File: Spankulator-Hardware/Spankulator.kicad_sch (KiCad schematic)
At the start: 100 parts, among them J1 3.5mm Jack, J12 Arduino Socket, J13 Arduino Socket, J2 2x5 Header, J3 3.5mm Jack, J4 3.5mm Jack, J5 3.5mm Jack, J6 3.5mm Jack, J7 2x5 Header, J9 Display Header, Q1 2N3904, SW1 Adj, SW2 Push Button, SW3 Push Button, SW4 Push Button, SW5 Push Button, SW6 Push Button, SW7 Push Button, SW8 Push Button, U1 TL072CP, U2 CD4013BE, U3 TL072CP, U4 MC78L05_TO92, U5 LP2950-3.3_TO92, U6 MAX7480, U7 MB85RC256, U8 MCP6002-E/P

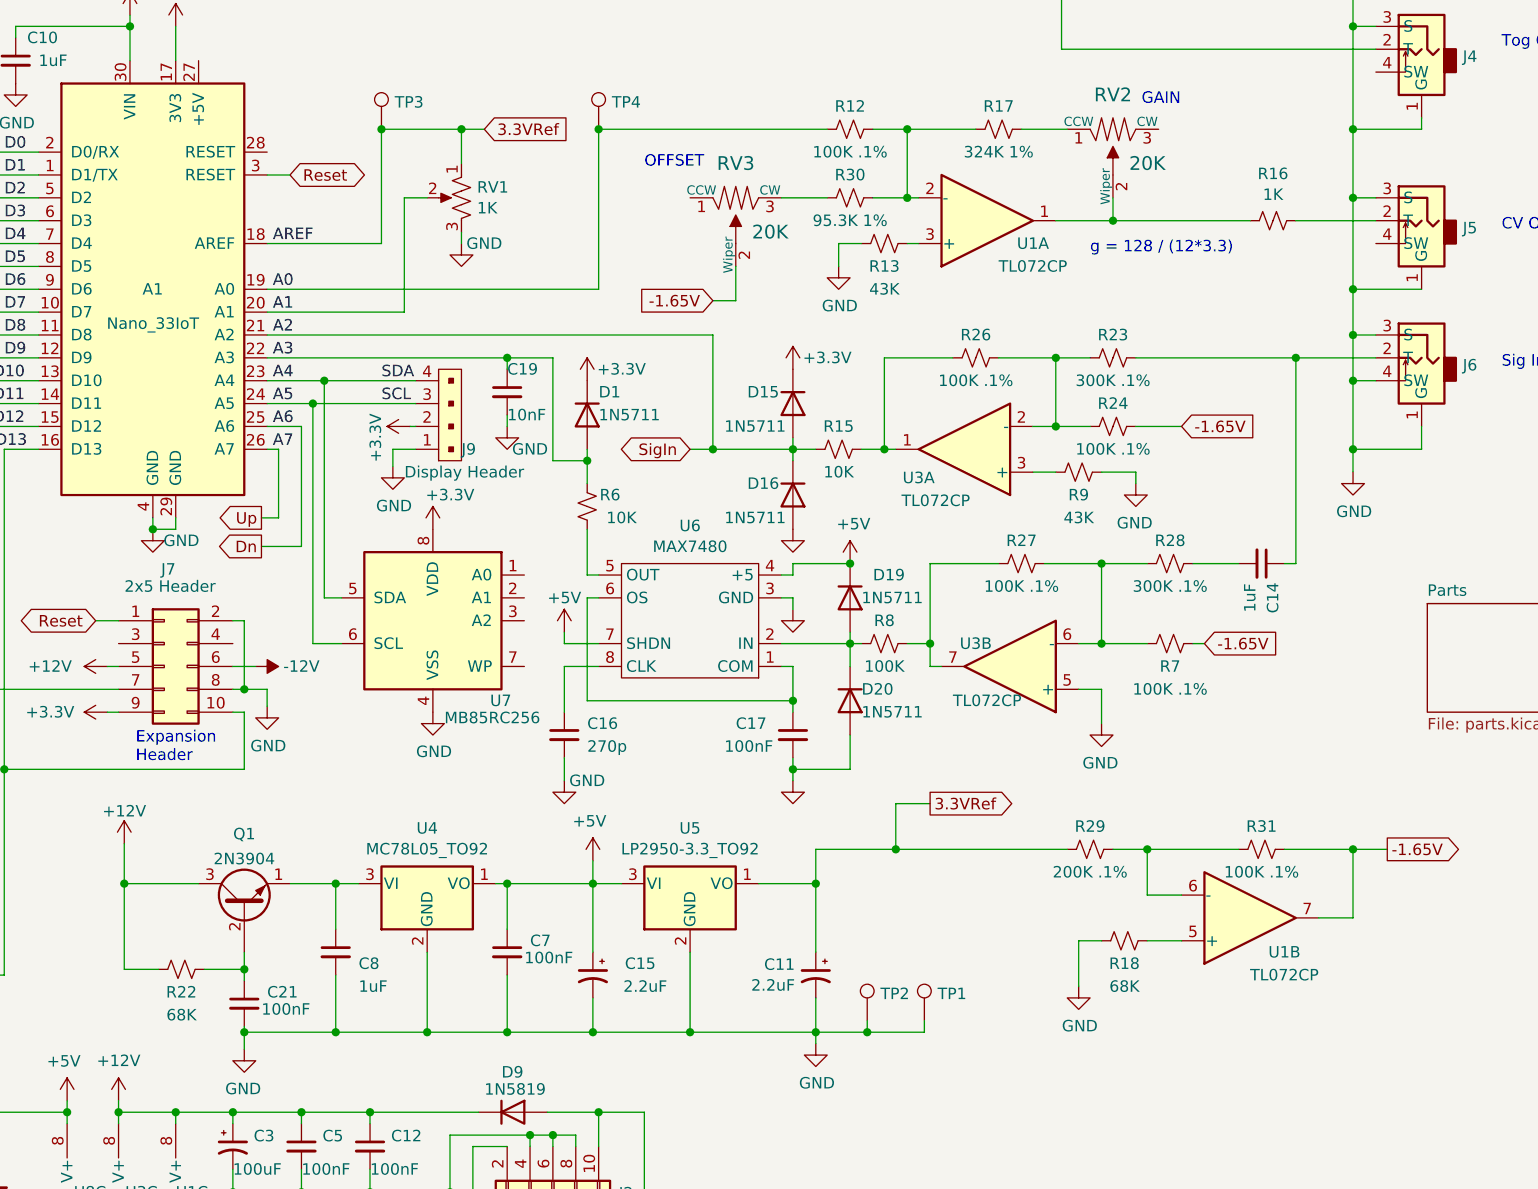
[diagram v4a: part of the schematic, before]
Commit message: Removes output resistor. Adjusts RC in reference filter
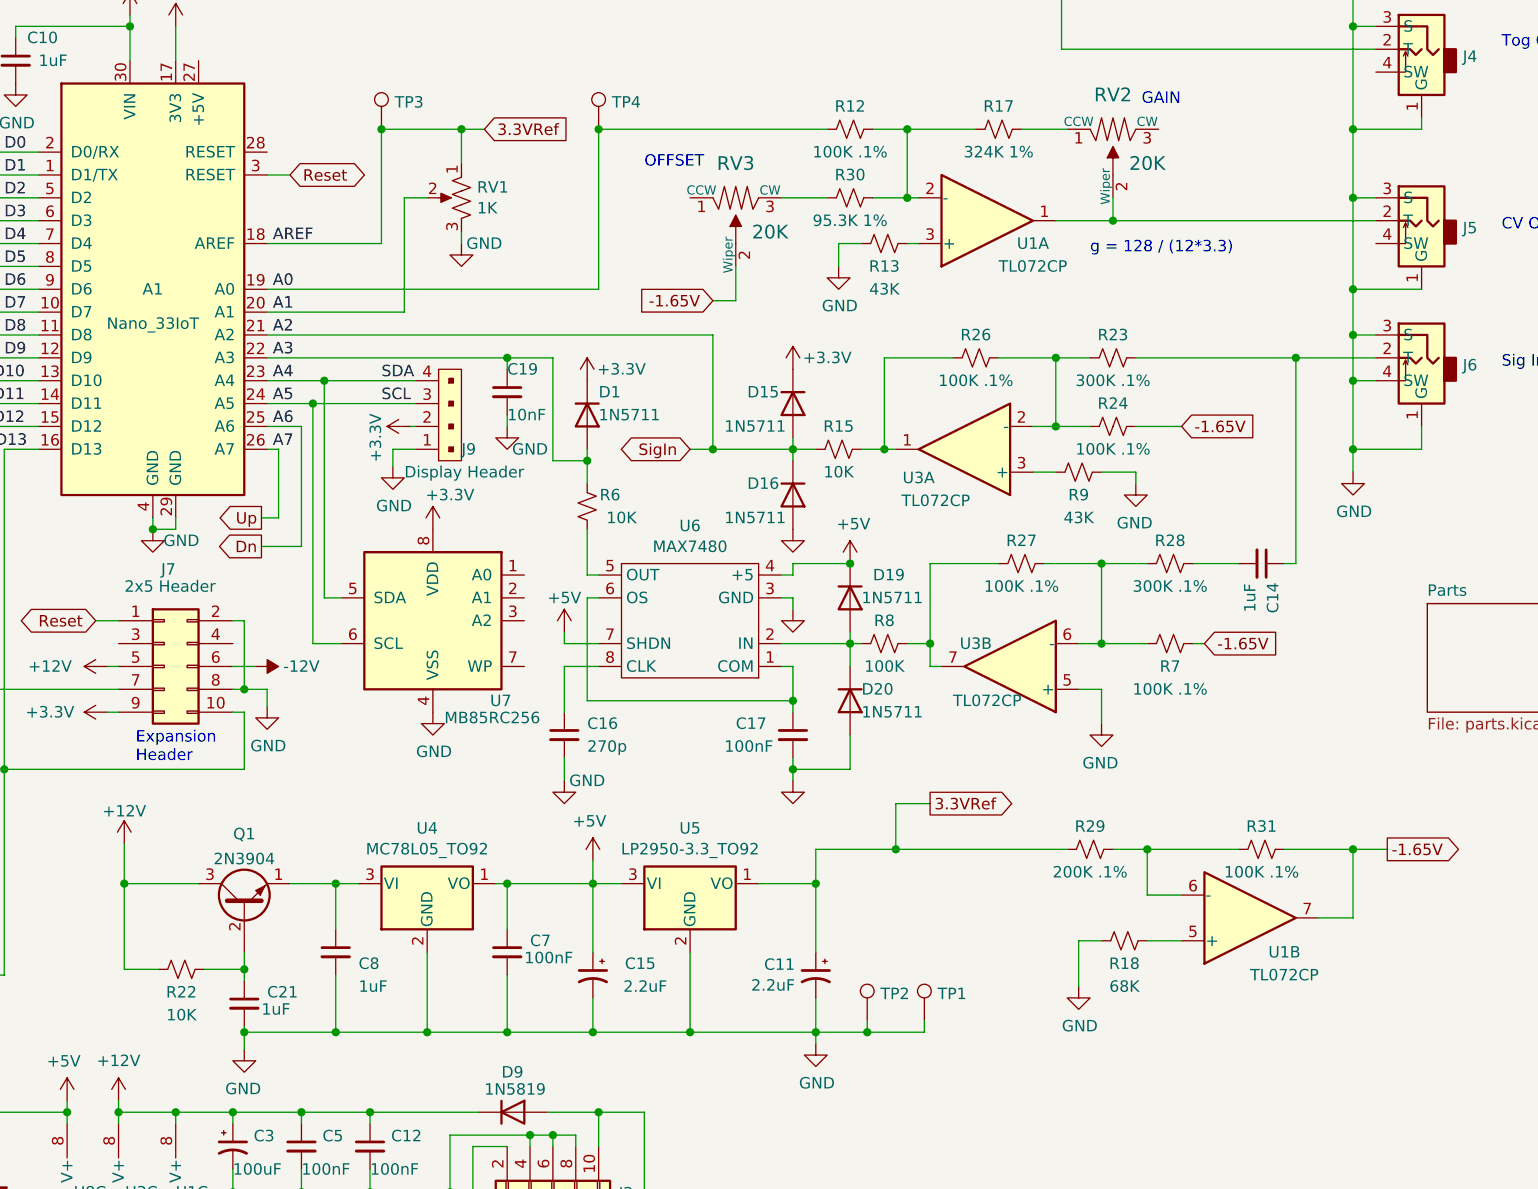
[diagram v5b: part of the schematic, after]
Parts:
- removed R16: 1K, Resistor_THT:R_Axial_DIN0207_L6.3mm_D2.5mm_P10.16mm_Horizontal, symbol Device:R_Small_US
- C21: value 100nF -> 1uF; Digi-Key Part 399-9877-1-ND -> 399-9886-1-ND; LCSC Part # C400087 -> C94708
- R22: value 68K -> 10K; Digi-Key Part CF14JT68K0CT-ND -> CF14JT10K0CT-ND; LCSC Part # C70783 -> C120103
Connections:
- net at RV2.2 (Wiper), U1.1: now also J5.2 (T)
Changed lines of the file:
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@@
     (stroke (width 0) (type default) (color 0 0 0 0))
   )
-  (wire (pts (xy 220.98 66.04) (xy 236.22 66.04))
-    (stroke (width 0) (type default) (color 0 0 0 0))
-  )
   (wire (pts (xy 219.71 93.98) (xy 223.52 93.98))
     (stroke (width 0) (type default) (color 0 0 0 0))
@@
     (stroke (width 0) (type default) (color 0 0 0 0))
   )
-  (wire (pts (xy 241.3 66.04) (xy 250.19 66.04))
+  (wire (pts (xy 220.98 66.04) (xy 250.19 66.04))
     (stroke (width 0) (type default) (color 0 0 0 0))
   )
@@
       (effects (font (size 1.27 1.27)) (justify left))
     )
-    (property "Value" "100nF" (id 1) (at 126.365 153.67 0)
+    (property "Value" "1uF" (id 1) (at 126.365 153.67 0)
       (effects (font (size 1.27 1.27)) (justify left))
     )
@@
       (effects (font (size 1.27 1.27)) hide)
     )
-    (property "Digi-Key Part" "399-9877-1-ND" (id 4) (at 124.46 153.035 0)
+    (property "Digi-Key Part" "399-9886-1-ND" (id 4) (at 124.46 153.035 0)
       (effects (font (size 1.27 1.27)) hide)
     )
-    (property "LCSC Part #" "C400087" (id 5) (at 124.46 153.035 0)
+    (property "LCSC Part #" "C94708" (id 5) (at 124.46 153.035 0)
       (effects (font (size 1.27 1.27)) hide)
     )
@@
     (in_bom yes) (on_board yes)
     (property "Reference" "R22" (id 0) (at 117.475 151.765 90))
-    (property "Value" "68K" (id 1) (at 117.475 154.305 90))
+    (property "Value" "10K" (id 1) (at 117.475 154.305 90))
     (property "Footprint" "Resistor_THT:R_Axial_DIN0207_L6.3mm_D2.5mm_P10.16mm_Horizontal" (id 2) (at 117.475 149.225 0)
       (effects (font (size 1.27 1.27)) hide)
@@
       (effects (font (size 1.27 1.27)) hide)
     )
-    (property "Digi-Key Part" "CF14JT68K0CT-ND" (id 4) (at 117.475 149.225 90)
+    (property "Digi-Key Part" "CF14JT10K0CT-ND" (id 4) (at 117.475 149.225 90)
       (effects (font (size 1.27 1.27)) hide)
     )
-    (property "LCSC Part #" "C70783" (id 5) (at 117.475 149.225 0)
-      (effects (font (size 1.27 1.27)) hide)
-    )
-    (pin "1")
-    (pin "2")
-  )
-  (symbol (lib_id "Device:R_Small_US") (at 238.76 66.04 270) (unit 1)
-    (in_bom yes) (on_board yes)
-    (property "Reference" "R16" (id 0) (at 238.76 60.833 90))
-    (property "Value" "1K" (id 1) (at 238.76 63.1444 90))
-    (property "Footprint" "Resistor_THT:R_Axial_DIN0207_L6.3mm_D2.5mm_P10.16mm_Horizontal" (id 2) (at 238.76 66.04 0)
-      (effects (font (size 1.27 1.27)) hide)
-    )
-    (property "Datasheet" "~" (id 3) (at 238.76 66.04 0)
-      (effects (font (size 1.27 1.27)) hide)
-    )
-    (property "Digi-Key Part" "CF14JT1K00CT-ND" (id 4) (at 238.76 66.04 90)
-      (effects (font (size 1.27 1.27)) hide)
-    )
-    (property "LCSC Part #" "C66649" (id 5) (at 238.76 66.04 0)
+    (property "LCSC Part #" "C120103" (id 5) (at 117.475 149.225 0)
       (effects (font (size 1.27 1.27)) hide)
     )
@@
     )
     (path "/83a7ca09-b4fd-493e-8bbb-bd08be746ed9"
-      (reference "C21") (unit 1) (value "100nF") (footprint "Capacitor_THT:C_Disc_D4.3mm_W1.9mm_P5.00mm")
+      (reference "C21") (unit 1) (value "1uF") (footprint "Capacitor_THT:C_Disc_D4.3mm_W1.9mm_P5.00mm")
     )
     (path "/00000000-0000-0000-0000-0000616dd95b"
@@
       (reference "R15") (unit 1) (value "10K") (footprint "Resistor_THT:R_Axial_DIN0207_L6.3mm_D2.5mm_P10.16mm_Horizontal")
     )
-    (path "/e07530a7-8a01-4924-9200-735d32c1129f"
-      (reference "R16") (unit 1) (value "1K") (footprint "Resistor_THT:R_Axial_DIN0207_L6.3mm_D2.5mm_P10.16mm_Horizontal")
-    )
     (path "/00000000-0000-0000-0000-00005f427c66"
       (reference "R17") (unit 1) (value "324K 1%") (footprint "Resistor_THT:R_Axial_DIN0207_L6.3mm_D2.5mm_P10.16mm_Horizontal")
@@
     )
     (path "/cbb1bb1c-2683-4a4d-a54f-78de9cd60431"
-      (reference "R22") (unit 1) (value "68K") (footprint "Resistor_THT:R_Axial_DIN0207_L6.3mm_D2.5mm_P10.16mm_Horizontal")
+      (reference "R22") (unit 1) (value "10K") (footprint "Resistor_THT:R_Axial_DIN0207_L6.3mm_D2.5mm_P10.16mm_Horizontal")
     )
     (path "/00000000-0000-0000-0000-00005f2994cf"

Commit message: New panel, new board.
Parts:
- C3, C4: footprint Capacitor_THT:CP_Radial_D8.0mm_P3.50mm -> Capacitor_THT:CP_Radial_D6.3mm_P2.50mm; Digi-Key Part 1189-3982-ND -> 10-ECE-A1CKA101ICT-ND; LCSC Part # C88859 -> C445356
- Q1, U5: footprint digikey-footprints:TO-92-3_Formed_Leads -> Package_TO_SOT_THT:TO-92-3_Formed_Leads
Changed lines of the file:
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@@
       (effects (font (size 1.27 1.27)) (justify left))
     )
-    (property "Footprint" "Capacitor_THT:CP_Radial_D8.0mm_P3.50mm" (id 2) (at 123.19 168.91 0)
+    (property "Footprint" "Capacitor_THT:CP_Radial_D6.3mm_P2.50mm" (id 2) (at 123.19 168.91 0)
       (effects (font (size 1.27 1.27)) hide)
     )
@@
       (effects (font (size 1.27 1.27)) hide)
     )
-    (property "Digi-Key Part" "1189-3982-ND" (id 4) (at 123.19 168.91 0)
+    (property "Digi-Key Part" "10-ECE-A1CKA101ICT-ND" (id 4) (at 123.19 168.91 0)
       (effects (font (size 1.27 1.27)) hide)
     )
-    (property "LCSC Part #" "C88859" (id 5) (at 123.19 168.91 0)
+    (property "LCSC Part #" "C445356" (id 5) (at 123.19 168.91 0)
       (effects (font (size 1.27 1.27)) hide)
     )
@@
       (effects (font (size 1.27 1.27)) (justify left))
     )
-    (property "Footprint" "Capacitor_THT:CP_Radial_D8.0mm_P3.50mm" (id 2) (at 123.19 177.8 0)
+    (property "Footprint" "Capacitor_THT:CP_Radial_D6.3mm_P2.50mm" (id 2) (at 123.19 177.8 0)
       (effects (font (size 1.27 1.27)) hide)
     )
@@
       (effects (font (size 1.27 1.27)) hide)
     )
-    (property "Digi-Key Part" "1189-3982-ND" (id 4) (at 123.19 177.8 0)
+    (property "Digi-Key Part" "10-ECE-A1CKA101ICT-ND" (id 4) (at 123.19 177.8 0)
       (effects (font (size 1.27 1.27)) hide)
     )
-    (property "LCSC Part #" "C88859" (id 5) (at 123.19 177.8 0)
+    (property "LCSC Part #" "C445356" (id 5) (at 123.19 177.8 0)
       (effects (font (size 1.27 1.27)) hide)
     )
@@
     (property "Reference" "U5" (id 0) (at 173.99 133.5532 0))
     (property "Value" "LP2950-3.3_TO92" (id 1) (at 173.99 135.8646 0))
-    (property "Footprint" "digikey-footprints:TO-92-3_Formed_Leads" (id 2) (at 173.99 133.985 0)
+    (property "Footprint" "Package_TO_SOT_THT:TO-92-3_Formed_Leads" (id 2) (at 173.99 133.985 0)
       (effects (font (size 1.27 1.27) italic) hide)
     )
@@
     (property "Reference" "Q1" (id 0) (at 124.46 134.1841 90))
     (property "Value" "2N3904" (id 1) (at 124.46 136.9592 90))
-    (property "Footprint" "digikey-footprints:TO-92-3_Formed_Leads" (id 2) (at 126.365 137.16 0)
+    (property "Footprint" "Package_TO_SOT_THT:TO-92-3_Formed_Leads" (id 2) (at 126.365 137.16 0)
       (effects (font (size 1.27 1.27) italic) (justify left) hide)
     )
@@
     )
     (path "/00000000-0000-0000-0000-00005cee41d1"
-      (reference "C3") (unit 1) (value "100uF") (footprint "Capacitor_THT:CP_Radial_D8.0mm_P3.50mm")
+      (reference "C3") (unit 1) (value "100uF") (footprint "Capacitor_THT:CP_Radial_D6.3mm_P2.50mm")
     )
     (path "/00000000-0000-0000-0000-00005cee5092"
-      (reference "C4") (unit 1) (value "100uF") (footprint "Capacitor_THT:CP_Radial_D8.0mm_P3.50mm")
+      (reference "C4") (unit 1) (value "100uF") (footprint "Capacitor_THT:CP_Radial_D6.3mm_P2.50mm")
     )
     (path "/00000000-0000-0000-0000-00005ceca0ce"
@@
     )
     (path "/82f88b33-a287-4e4b-8286-fcbdf9dee6f1"
-      (reference "Q1") (unit 1) (value "2N3904") (footprint "digikey-footprints:TO-92-3_Formed_Leads")
+      (reference "Q1") (unit 1) (value "2N3904") (footprint "Package_TO_SOT_THT:TO-92-3_Formed_Leads")
     )
     (path "/00000000-0000-0000-0000-00005ce0a0b6"
@@
     )
     (path "/00000000-0000-0000-0000-00006038f82e"
-      (reference "U5") (unit 1) (value "LP2950-3.3_TO92") (footprint "digikey-footprints:TO-92-3_Formed_Leads")
+      (reference "U5") (unit 1) (value "LP2950-3.3_TO92") (footprint "Package_TO_SOT_THT:TO-92-3_Formed_Leads")
     )
     (path "/00000000-0000-0000-0000-00006045cf3c"
